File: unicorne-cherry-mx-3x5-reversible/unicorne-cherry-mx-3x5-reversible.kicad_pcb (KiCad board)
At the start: 2 copper layers, 114.7 x 91.4 mm, 84 parts, among them J1 MJ-4PP-9, J2 Nice!View, J3 Conn_01x02, J4 Conn_01x03, SW1 SW_MX_HS, SW10 SW_MX_HS, SW11 SW_MX_HS, SW12 SW_MX_HS, SW13 SW_MX_HS, SW14 SW_MX_HS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

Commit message: amend PCB
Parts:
- moved J4 18.9 mm to (174.1, 82.4)
- renumbered Left to R1, Right to R2
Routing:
- net col3: track 226.1 -> 140.9 mm, vias 1 -> 2
- net col4: track 210.2 -> 130.5 mm, vias 1 -> 2
- net col1: track 220.8 -> 151.1 mm, vias 2 -> 1
- net col2: track 247.6 -> 178.6 mm
- net col0: track 238.0 -> 176.8 mm
- net row1: track 141.8 -> 112.3 mm
- net LED: track 66.7 -> 45.4 mm, vias 4 -> 2
- net Net-(L10-DOUT): track 44.4 -> 28.0 mm
- net Net-(D4-A): track 19.9 -> 3.81 mm
- net Net-(D16-A): track 19.9 -> 3.92 mm
- net Net-(D5-A): track 19.9 -> 3.93 mm
- net Net-(D14-A): track 19.8 -> 3.79 mm
- net Net-(D3-A): track 19.8 -> 3.81 mm
- net Net-(D8-A): track 19.6 -> 3.59 mm
- net Net-(D13-A): track 19.8 -> 3.79 mm
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
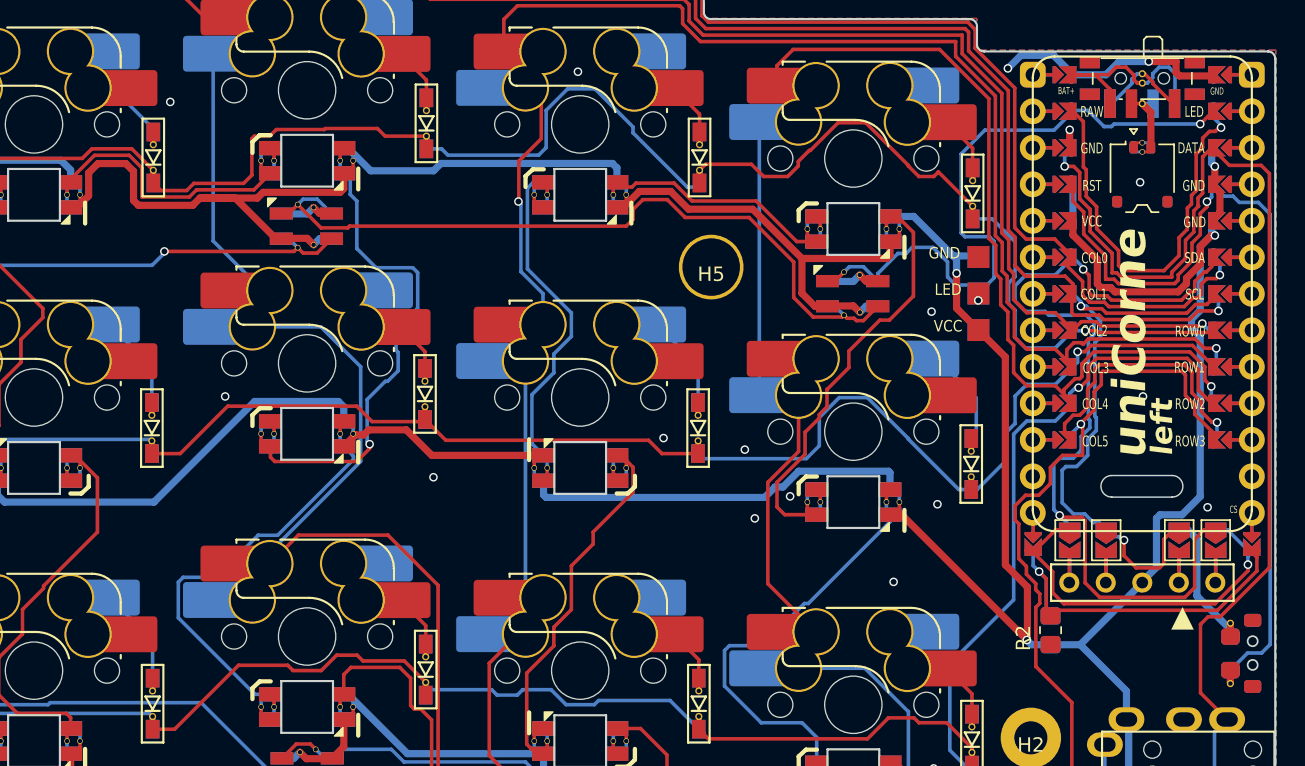
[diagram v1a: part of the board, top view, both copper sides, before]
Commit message: amend silkscreen
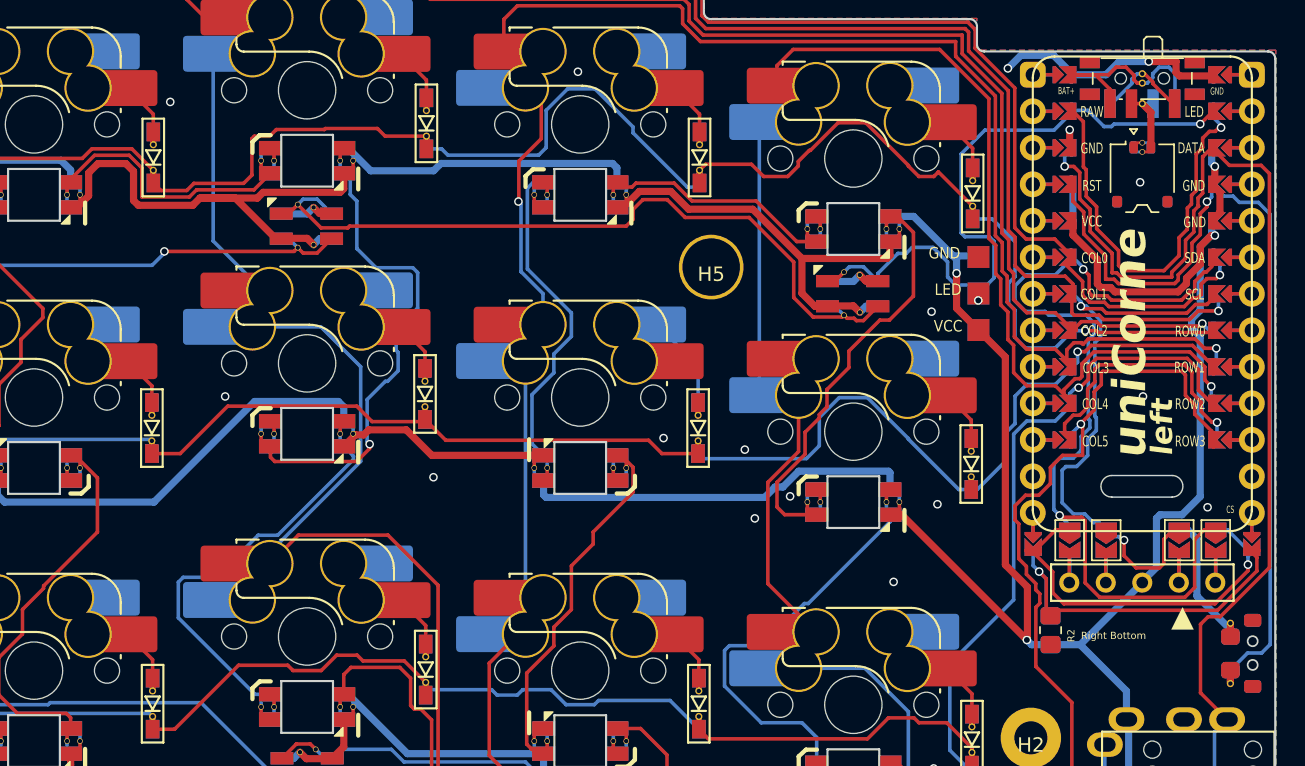
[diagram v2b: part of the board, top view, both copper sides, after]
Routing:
- net Net-(D12-A): track 6.84 -> 3.79 mm
- net Net-(D7-A): track 6.65 -> 3.59 mm
- net Net-(D10-A): track 6.34 -> 3.72 mm
- net Net-(D2-A): track 5.71 -> 3.81 mm
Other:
- board text added: "Left Bottom"
- board text added: "Right Bottom"
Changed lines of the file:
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@@
     (property "ki_keywords" "R res resistor")
     (attr smd)
-    (fp_text reference "R2" (at -0.54 -1.89 90) (layer "F.SilkS")
-        (effects (font (size 1 1) (thickness 0.15)))
+    (fp_text reference "R2" (at -0.38 1.43 90) (layer "F.SilkS")
+        (effects (font (size 0.5 0.5) (thickness 0.075)))
     )
     (fp_text value "10k" (at 0 1.65 90) (layer "F.Fab") hide
@@
         (effects (font (size 0.75 0.5) (thickness 0.125)) (justify mirror))
     )
-    (fp_text user "CS" (at -6.19 13.68) (layer "B.SilkS")
+    (fp_text user "CS" (at -5.92 13.5) (layer "B.SilkS")
         (effects (font (size 0.5 0.3) (thickness 0.075)) (justify mirror))
     )
@@
         (effects (font (size 0.75 0.5) (thickness 0.125)))
     )
-    (fp_text user "CS" (at 6.5 13.6892) (layer "F.SilkS")
+    (fp_text user "CS" (at 6.2724 13.6892) (layer "F.SilkS")
         (effects (font (size 0.5 0.3) (thickness 0.075)))
     )
@@
     (fp_arc (start -4.035 6.74) (mid -5.449216 6.154216) (end -6.035 4.74)
       (stroke (width 0.15) (type solid)) (layer "F.SilkS"))
-    (fp_arc (start -0.149824 2.69) (mid -1.620517 2.173417) (end -2.444146 0.85)
+    (fp_arc (start -0.149824 2.69) (mid -1.620518 2.173417) (end -2.444146 0.85)
       (stroke (width 0.15) (type solid)) (layer "F.SilkS"))
     (fp_arc (start 4.415 2.69) (mid 4.768554 2.836447) (end 4.915 3.19)
@@
     (fp_arc (start -6.997236 -6.498884) (mid -6.850789 -6.852437) (end -6.497236 -6.998884)
       (stroke (width 0.05) (type solid)) (layer "Eco2.User"))
-    (fp_arc (start -6.5 7) (mid -6.853553 6.853553) (end -7 6.5)
+    (fp_arc (start -6.5 7) (mid -6.853553 6.853554) (end -7 6.5)
       (stroke (width 0.05) (type solid)) (layer "Eco2.User"))
     (fp_arc (start -6.449824 6.98978) (mid -6.803377 6.843333) (end -6.949824 6.48978)
@@
     (fp_arc (start -0.2 2.70022) (mid -1.670694 2.183637) (end -2.494322 0.86022)
       (stroke (width 0.15) (type solid)) (layer "F.SilkS"))
-    (fp_arc (start 4.364824 2.70022) (mid 4.718391 2.846671) (end 4.864824 3.20022)
+    (fp_arc (start 4.364824 2.70022) (mid 4.718381 2.846662) (end 4.864824 3.20022)
       (stroke (width 0.15) (type solid)) (layer "F.SilkS"))
     (fp_line (start -14.2875 -9.525) (end -14.2875 9.525)
@@
     (property "ki_keywords" "R res resistor")
     (attr smd)
-    (fp_text reference "R1" (at 0.74 -1.89 90) (layer "B.SilkS")
-        (effects (font (size 1 1) (thickness 0.15)) (justify mirror))
+    (fp_text reference "R1" (at -0.34 1.44 90) (layer "B.SilkS")
+        (effects (font (size 0.5 0.5) (thickness 0.075) bold) (justify mirror))
     )
     (fp_text value "10k" (at 0 -1.65 90) (layer "B.Fab") hide
@@
     (effects (font (size 1 1) (thickness 0.125)) (justify left mirror))
   )
+  (gr_text "Left Bottom" (at 183.45 108.74) (layer "B.SilkS")
+    (effects (font (size 0.5 0.5) (thickness 0.075)) (justify mirror))
+  )
   (gr_text "GND" (at 171.94 87.21) (layer "B.SilkS")
     (effects (font (size 0.8 0.7) (thickness 0.125)) (justify mirror))
@@
     (effects (font (size 0.8 0.7) (thickness 0.125)) (justify mirror))
   )
+  (gr_text "Right Bottom" (at 183.45 108.74) (layer "F.SilkS")
+    (effects (font (size 0.5 0.5) (thickness 0.075)))
+  )
   (gr_text "VCC" (at 171.94 87.21) (layer "F.SilkS")
     (effects (font (size 0.8 0.7) (thickness 0.125)))
@@
   (segment (start 192.7725 109.95) (end 193.75 109.95) (width 0.25) (layer "B.Cu") (net 35))
   (segment (start 191.1034 78.1642) (end 190.2784 77.3392) (width 0.25) (layer "B.Cu") (net 35))
-  (segment (start 113.81482 70.64482) (end 116.65 73.48) (width 0.25) (layer "B.Cu") (net 36))
-  (segment (start 112.109824 70.64482) (end 113.81482 70.64482) (width 0.25) (layer "B.Cu") (net 36))
+  (segment (start 114.834824 70.64482) (end 116.65 72.459996) (width 0.25) (layer "F.Cu") (net 36))
+  (segment (start 116.65 72.459996) (end 116.65 73.7) (width 0.25) (layer "F.Cu") (net 36))
   (segment (start 135.65 70.084996) (end 135.65 71.325) (width 0.25) (layer "F.Cu") (net 37))
   (segment (start 133.834824 68.26982) (end 135.65 70.084996) (width 0.25) (layer "F.Cu") (net 37))
@@
   (segment (start 95.834824 94.39482) (end 97.55 96.109996) (width 0.25) (layer "F.Cu") (net 41))
   (segment (start 97.55 96.109996) (end 97.55 97.275) (width 0.25) (layer "F.Cu") (net 41))
-  (segment (start 113.615 87.0946) (end 116.55 90.0296) (width 0.25) (layer "B.Cu") (net 42))
-  (segment (start 116.55 90.0296) (end 116.55 92.525) (width 0.25) (layer "B.Cu") (net 42))
+  (segment (start 114.834824 89.64482) (end 116.55 91.359996) (width 0.25) (layer "F.Cu") (net 42))
+  (segment (start 116.55 91.359996) (end 116.55 92.525) (width 0.25) (layer "F.Cu") (net 42))
   (segment (start 135.55 88.984996) (end 135.55 90.15) (width 0.25) (layer "F.Cu") (net 43))
   (segment (start 133.834824 87.26982) (end 135.55 88.984996) (width 0.25) (layer "F.Cu") (net 43))
   (segment (start 151.615 87.035) (end 154.55 89.97) (width 0.25) (layer "B.Cu") (net 44))
   (segment (start 154.55 89.97) (end 154.55 92.525) (width 0.25) (layer "B.Cu") (net 44))
-  (segment (start 172.59 90.894169) (end 173.9 92.204169) (width 0.25) (layer "B.Cu") (net 45))
-  (segment (start 172.59 90.89) (end 172.59 90.894169) (width 0.25) (layer "B.Cu") (net 45))
-  (segment (start 173.9 92.204169) (end 173.9 94.675) (width 0.25) (layer "B.Cu") (net 45))
-  (segment (start 171.1696 89.4696) (end 172.59 90.89) (width 0.25) (layer "B.Cu") (net 45))
+  (segment (start 173.55 93.734996) (end 173.55 95.025) (width 0.25) (layer "F.Cu") (net 45))
+  (segment (start 171.834824 92.01982) (end 173.55 93.734996) (width 0.25) (layer "F.Cu") (net 45))
   (segment (start 95.834824 113.39482) (end 97.6 115.159996) (width 0.25) (layer "F.Cu") (net 46))
   (segment (start 97.6 115.159996) (end 97.6 116.45) (width 0.25) (layer "F.Cu") (net 46))
-  (segment (start 116.6 109.0796) (end 116.6 111.7) (width 0.25) (layer "B.Cu") (net 47))
-  (segment (start 113.615 106.0946) (end 116.6 109.0796) (width 0.25) (layer "B.Cu") (net 47))
+  (segment (start 116.6 110.409996) (end 116.6 111.7) (width 0.25) (layer "F.Cu") (net 47))
+  (segment (start 114.834824 108.64482) (end 116.6 110.409996) (width 0.25) (layer "F.Cu") (net 47))
   (segment (start 135.6 108.034996) (end 135.6 109.325) (width 0.25) (layer "F.Cu") (net 48))
   (segment (start 133.834824 106.26982) (end 135.6 108.034996) (width 0.25) (layer "F.Cu") (net 48))
